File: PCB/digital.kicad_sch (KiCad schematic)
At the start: 34 parts, among them J13 JTAG, J14 FINAL_CARRERA_UP, J15 FINAL_CARRERA_DOWN, J3 ICSP, J4 CAN, J6 USART, J7 SPI, J8 RFID_COAX, U2 PIC32MK0256MCJ048-I/Y8X, U3 TCAN334D, Y1 ECS-3225SMV-080-GP-TR, Y2 ECS-3225SMV-080-GP-TR

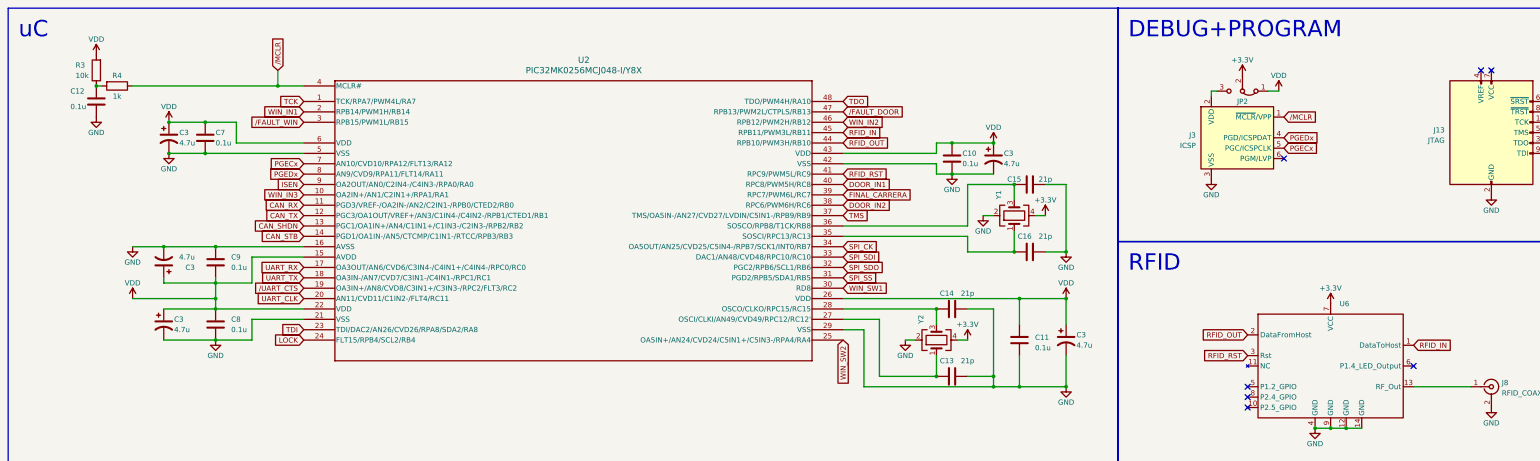
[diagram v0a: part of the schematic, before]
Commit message: power plane done
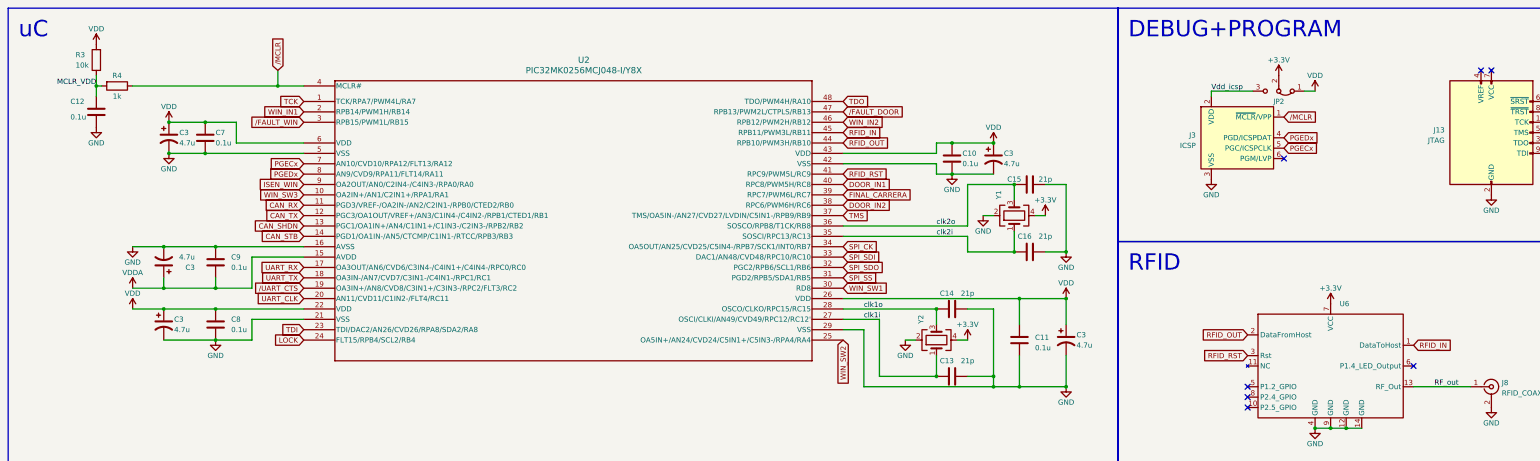
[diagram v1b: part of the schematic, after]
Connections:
- net VDD: no longer C3.1, C9.2, U2.15 (AVDD)
- net MCLR_VDD: now reaches C12.1, R3.1, R4.2
- net RF_out: now reaches J8.1 (In), U6.13 (RF_Out)
- net clk2i: now reaches C16.1, U2.35 (SOSCI/RPC13/RC13), Y1.1
- net clk2o: now reaches C15.1, U2.36 (SOSCO/RPB8/T1CK/RB8), Y1.3
- net clk1i: now reaches C13.1, U2.27 (OSCI/CLKI/AN49/CVD49/RPC12/RC12'), Y2.1
- net clk1o: now reaches C14.1, U2.28 (OSCO/CLKO/RPC15/RC15), Y2.3
- net Vdd_icsp: now reaches J3.2 (VDD), JP2.3 (B)
- net ISEN renamed ISEN_WIN
- net WIN_IN3 renamed WIN_SW3
- new net VDDA: C3.1, C9.2, U2.15 (AVDD)
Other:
- moved on the sheet: C12, JP2, R3

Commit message: start digital
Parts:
- added R1 (x2): 0, symbol Device:R
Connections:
- net GND: now also R1.2; no longer C3.2, C9.1, U2.16 (AVSS)
- net VDD: now also R1.2
- net VDDA: now also R1.1
- new net GNDA: C3.2, C9.1, R1.1, U2.16 (AVSS)
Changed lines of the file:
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@@
+    (fill (type none))
+  )
+  (rectangle (start 12.7 104.14) (end 34.29 129.54)
+    (stroke (width 0) (type default))
     (fill (type none))
   )
@@
     )
   )
+  (symbol (lib_id "Device:R") (at 22.86 113.03 90) (unit 1)
+    (in_bom yes) (on_board yes) (dnp no)
+    (property "Reference" "R1" (at 22.86 110.49 90)
+      (effects (font (size 1.27 1.27)))
+    )
+    (property "Value" "0" (at 22.86 115.57 90)
+      (effects (font (size 1.27 1.27)))
+    )
+    (property "Footprint" "" (at 22.86 114.808 90)
+      (effects (font (size 1.27 1.27)) hide)
+    )
+    (property "Datasheet" "~" (at 22.86 113.03 0)
+      (effects (font (size 1.27 1.27)) hide)
+    )
+    (pin "1")
+    (pin "2")
+    (instances
+      (project "DIJOUS_4_PORTES"
+        (path "/69b34976-047e-478e-bd76-9b6ef0dba356/0e58b9bb-7a32-4563-ae50-f5e325ba8348"
+          (reference "R1") (unit 1)
+        )
+        (path "/69b34976-047e-478e-bd76-9b6ef0dba356/6b83d062-cc2b-4223-9dc9-bddc64623104"
+          (reference "R2") (unit 1)
+        )
+      )
+    )
+  )
+  (symbol (lib_id "power:VDDA") (at 19.05 113.03 0) (unit 1)
+    (in_bom yes) (on_board yes) (dnp no) (fields_autoplaced)
+    (property "Reference" "#PWR08" (at 19.05 116.84 0)
+      (effects (font (size 1.27 1.27)) hide)
+    )
+    (property "Value" "VDDA" (at 19.05 109.22 0)
+      (effects (font (size 1.27 1.27)))
+    )
+    (property "Footprint" "" (at 19.05 113.03 0)
+      (effects (font (size 1.27 1.27)) hide)
+    )
+    (property "Datasheet" "" (at 19.05 113.03 0)
+      (effects (font (size 1.27 1.27)) hide)
+    )
+    (pin "1")
+    (instances
+      (project "DIJOUS_4_PORTES"
+        (path "/69b34976-047e-478e-bd76-9b6ef0dba356/6b83d062-cc2b-4223-9dc9-bddc64623104"
+          (reference "#PWR08") (unit 1)
+        )
+      )
+    )
+  )
   (symbol (lib_id "Device:R") (at 39.37 31.75 270) (unit 1)
     (in_bom yes) (on_board yes) (dnp no)
@@
         (path "/69b34976-047e-478e-bd76-9b6ef0dba356/6b83d062-cc2b-4223-9dc9-bddc64623104"
           (reference "R4") (unit 1)
-        )
-      )
-    )
-  )
-  (symbol (lib_id "power:GND") (at 43.18 71.12 0) (unit 1)
-    (in_bom yes) (on_board yes) (dnp no)
-    (property "Reference" "#PWR015" (at 43.18 77.47 0)
-      (effects (font (size 1.27 1.27)) hide)
-    )
-    (property "Value" "GND" (at 43.18 74.93 0)
-      (effects (font (size 1.27 1.27)))
-    )
-    (property "Footprint" "" (at 43.18 71.12 0)
-      (effects (font (size 1.27 1.27)) hide)
-    )
-    (property "Datasheet" "" (at 43.18 71.12 0)
-      (effects (font (size 1.27 1.27)) hide)
-    )
-    (pin "1")
-    (instances
-      (project "DIJOUS_4_PORTES"
-        (path "/69b34976-047e-478e-bd76-9b6ef0dba356/6b83d062-cc2b-4223-9dc9-bddc64623104"
-          (reference "#PWR015") (unit 1)
         )
       )
@@
     )
   )
+  (symbol (lib_id "power:GNDA") (at 19.05 120.65 0) (unit 1)
+    (in_bom yes) (on_board yes) (dnp no)
+    (property "Reference" "#PWR07" (at 19.05 127 0)
+      (effects (font (size 1.27 1.27)) hide)
+    )
+    (property "Value" "GNDA" (at 19.05 124.46 0)
+      (effects (font (size 1.27 1.27)))
+    )
+    (property "Footprint" "" (at 19.05 120.65 0)
+      (effects (font (size 1.27 1.27)) hide)
+    )
+    (property "Datasheet" "" (at 19.05 120.65 0)
+      (effects (font (size 1.27 1.27)) hide)
+    )
+    (pin "1")
+    (instances
+      (project "DIJOUS_4_PORTES"
+        (path "/69b34976-047e-478e-bd76-9b6ef0dba356/6b83d062-cc2b-4223-9dc9-bddc64623104"
+          (reference "#PWR07") (unit 1)
+        )
+      )
+    )
+  )
   (symbol (lib_id "power:GND") (at 271.78 105.41 0) (unit 1)
     (in_bom yes) (on_board yes) (dnp no)
@@
         (path "/69b34976-047e-478e-bd76-9b6ef0dba356/6b83d062-cc2b-4223-9dc9-bddc64623104"
           (reference "C29") (unit 1)
+        )
+      )
+    )
+  )
+  (symbol (lib_id "power:GND") (at 26.67 120.65 0) (unit 1)
+    (in_bom yes) (on_board yes) (dnp no)
+    (property "Reference" "#PWR09" (at 26.67 127 0)
+      (effects (font (size 1.27 1.27)) hide)
+    )
+    (property "Value" "GND" (at 26.67 124.46 0)
+      (effects (font (size 1.27 1.27)))
+    )
+    (property "Footprint" "" (at 26.67 120.65 0)
+      (effects (font (size 1.27 1.27)) hide)
+    )
+    (property "Datasheet" "" (at 26.67 120.65 0)
+      (effects (font (size 1.27 1.27)) hide)
+    )
+    (pin "1")
+    (instances
+      (project "DIJOUS_4_PORTES"
+        (path "/69b34976-047e-478e-bd76-9b6ef0dba356/6b83d062-cc2b-4223-9dc9-bddc64623104"
+          (reference "#PWR09") (unit 1)
         )
       )
@@
         (path "/69b34976-047e-478e-bd76-9b6ef0dba356/6b83d062-cc2b-4223-9dc9-bddc64623104"
           (reference "J3") (unit 1)
+        )
+      )
+    )
+  )
+  (symbol (lib_id "power:VDD") (at 26.67 113.03 0) (unit 1)
+    (in_bom yes) (on_board yes) (dnp no)
+    (property "Reference" "#PWR015" (at 26.67 116.84 0)
+      (effects (font (size 1.27 1.27)) hide)
+    )
+    (property "Value" "VDD" (at 26.67 109.22 0)
+      (effects (font (size 1.27 1.27)))
+    )
+    (property "Footprint" "" (at 26.67 113.03 0)
+      (effects (font (size 1.27 1.27)) hide)
+    )
+    (property "Datasheet" "" (at 26.67 113.03 0)
+      (effects (font (size 1.27 1.27)) hide)
+    )
+    (pin "1")
+    (instances
+      (project "DIJOUS_4_PORTES"
+        (path "/69b34976-047e-478e-bd76-9b6ef0dba356/6b83d062-cc2b-4223-9dc9-bddc64623104"
+          (reference "#PWR015") (unit 1)
         )
       )
@@
         )
       )
+    )
+  )
+  (symbol (lib_id "power:GNDA") (at 43.18 71.12 0) (unit 1)
+    (in_bom yes) (on_board yes) (dnp no)
+    (property "Reference" "#PWR04" (at 43.18 77.47 0)
+      (effects (font (size 1.27 1.27)) hide)
+    )
+    (property "Value" "GNDA" (at 43.18 74.93 0)
+      (effects (font (size 1.27 1.27)))
+    )
+    (property "Footprint" "" (at 43.18 71.12 0)
+      (effects (font (size 1.27 1.27)) hide)
+    )
+    (property "Datasheet" "" (at 43.18 71.12 0)
+      (effects (font (size 1.27 1.27)) hide)
+    )
+    (pin "1")
+    (instances
+      (project "DIJOUS_4_PORTES"
+        (path "/69b34976-047e-478e-bd76-9b6ef0dba356/6b83d062-cc2b-4223-9dc9-bddc64623104"
+          (reference "#PWR04") (unit 1)
+        )
+      )
+    )
+  )
+  (symbol (lib_id "Device:R") (at 22.86 120.65 90) (unit 1)
+    (in_bom yes) (on_board yes) (dnp no)
+    (property "Reference" "R1" (at 22.86 118.11 90)
+      (effects (font (size 1.27 1.27)))
+    )
+    (property "Value" "0" (at 22.86 123.19 90)
+      (effects (font (size 1.27 1.27)))
+    )
+    (property "Footprint" "" (at 22.86 122.428 90)
+      (effects (font (size 1.27 1.27)) hide)
+    )
+    (property "Datasheet" "~" (at 22.86 120.65 0)
+      (effects (font (size 1.27 1.27)) hide)
+    )
+    (pin "1")
+    (pin "2")
+    (instances
+      (project "DIJOUS_4_PORTES"
+        (path "/69b34976-047e-478e-bd76-9b6ef0dba356/0e58b9bb-7a32-4563-ae50-f5e325ba8348"
+          (reference "R1") (unit 1)
+        )
+        (path "/69b34976-047e-478e-bd76-9b6ef0dba356/6b83d062-cc2b-4223-9dc9-bddc64623104"
+          (reference "R9") (unit 1)
+        )
+      )

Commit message: changed clks, pwr
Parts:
- removed C13, C14, C15, C16: 21p, Capacitor_SMD:C_01005_0402Metric, symbol Device:C
- removed J13: JTAG, Connector_IDC:IDC-Header_2x05_P2.54mm_Vertical, symbol Connector:AVR-JTAG-10
- removed JP2: Jumper_3_Bridged12, Connector_PinHeader_1.00mm:PinHeader_1x03_P1.00mm_Vertical, symbol Jumper:Jumper_3_Bridged12
- removed R1 (x2): 0, symbol Device:R
- removed Y1, Y2: ECS-3225SMV-080-GP-TR, kicad_models:OSC_ECS-3225SMV-080-GP-TR, symbol Device:Crystal_GND24
- added Y1: ASZKDV-32.768KHZ-L-T3, kicad_models:ASZKDV_ABR, symbol ASZKDV_ABR:ASZKDV-32.768KHZ-L-T3
- added Y2: ECS-3225SMV-080-GP-TR, kicad_models:OSC_ECS-3225SMV-080-GP-TR, symbol ECS-3225SMV-080-GP-TR:ECS-3225SMV-080-GP-TR
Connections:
- net FINAL_CARRERA is gone; now on net FINAL_CARRERA_UP: U2.39 (RPC7/PWM6L/RC7)
- net GNDA is gone; now on net GND: C3.2, C9.1, U2.16 (AVSS)
- net VDD is gone; now on net +3.3V: C10.1, C11.1, C3.1, C3.1, C3.1, C3.1, C7.1, C8.1, R3.2, U2.22 (VDD), U2.26 (VDD), U2.43 (VDD), U2.6 (VDD)
- net VDDA is gone; now on net +3.3V: C3.1, C9.2, U2.15 (AVDD)
- net Vdd_icsp is gone; now on net +3.3V: J3.2 (VDD)
- net clk2o is gone; now on net FINAL_CARRERA_DOWN: U2.36 (SOSCO/RPB8/T1CK/RB8)
- net +3.3V: now also Y1.3 (OE), Y1.4 (VDD), Y2.4 (VDD)
- net GND: now also Y1.2 (GND), Y2.2 (GND)
- net clk1i: now also Y2.3 (OUTPUT)
- net clk2i: now also Y1.1 (OUTPUT)
- net clk1o: no longer names the net of U2.28 (OSCO/CLKO/RPC15/RC15)
- no-connect marks 16 -> 15
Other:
- moved on the sheet: C11, C3

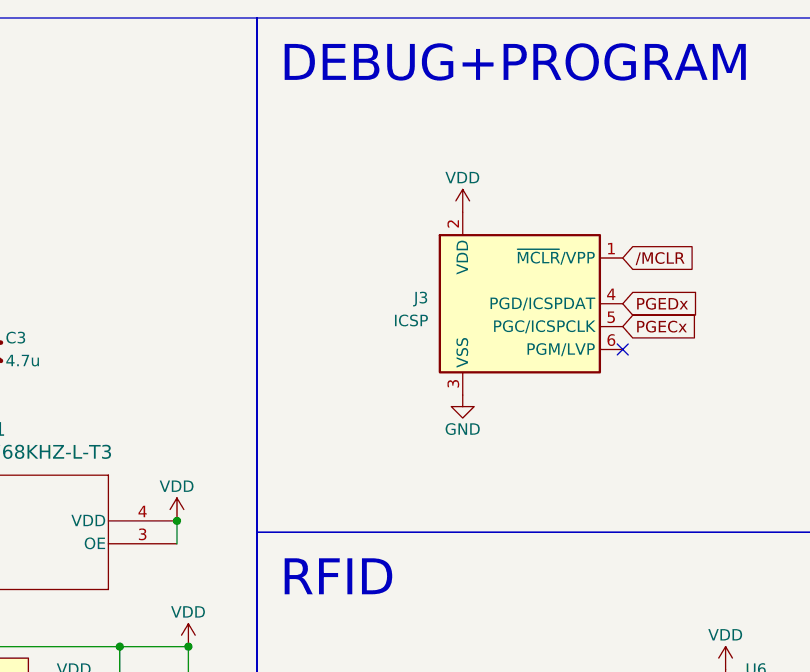
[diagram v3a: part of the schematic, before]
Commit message: canvis a sortides de potencia
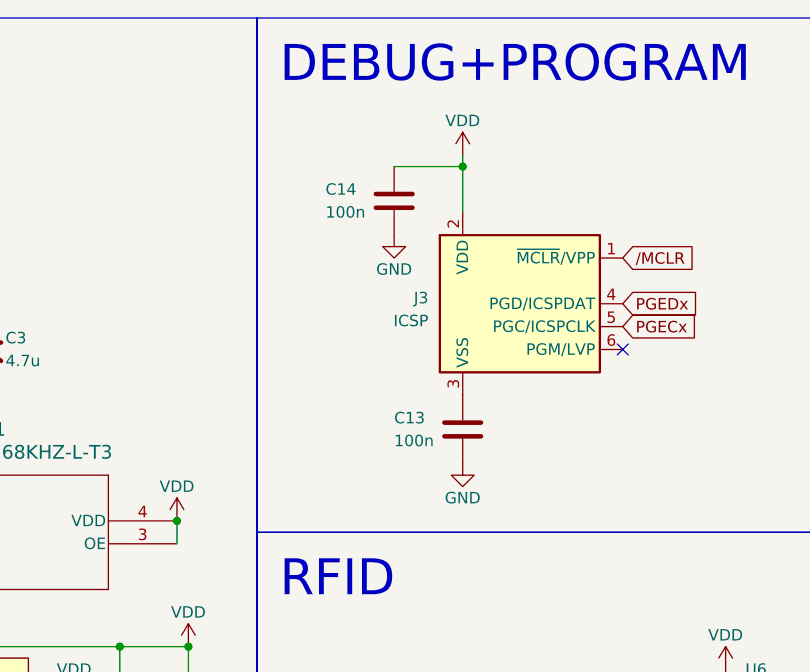
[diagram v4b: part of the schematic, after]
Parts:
- added C13, C14: 100n, Capacitor_SMD:C_0805_2012Metric, symbol Device:C
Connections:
- net +3.3V: now also C14.2
- net GND: now also C13.1, C14.1; no longer J3.3 (VSS)
- new net: C13.2, J3.3 (VSS)
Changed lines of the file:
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@@
   (junction (at 254 45.72) (diameter 0) (color 0 0 0 0)
+  )
+  (junction (at 307.34 29.21) (diameter 0) (color 0 0 0 0)
   )
   (junction (at 336.55 115.57) (diameter 0) (color 0 0 0 0)
@@
     (stroke (width 0) (type default))
   )
+  (wire (pts (xy 307.34 29.21) (xy 307.34 34.29))
+    (stroke (width 0) (type default))
+  )
   (wire (pts (xy 19.05 120.65) (xy 26.67 120.65))
     (stroke (width 0) (type default))
@@
     (stroke (width 0) (type default))
   )
+  (wire (pts (xy 299.72 29.21) (xy 307.34 29.21))
+    (stroke (width 0) (type default))
+  )
   (wire (pts (xy 34.29 29.21) (xy 34.29 31.75))
     (stroke (width 0) (type default))
@@
   )
   (wire (pts (xy 68.58 40.64) (xy 68.58 45.72))
+    (stroke (width 0) (type default))
+  )
+  (wire (pts (xy 307.34 27.94) (xy 307.34 29.21))
     (stroke (width 0) (type default))
   )
@@
     )
   )
+  (symbol (lib_id "power:GND") (at 299.72 36.83 0) (unit 1)
+    (in_bom yes) (on_board yes) (dnp no)
+    (property "Reference" "#PWR029" (at 299.72 43.18 0)
+      (effects (font (size 1.27 1.27)) hide)
+    )
+    (property "Value" "GND" (at 299.72 40.64 0)
+      (effects (font (size 1.27 1.27)))
+    )
+    (property "Footprint" "" (at 299.72 36.83 0)
+      (effects (font (size 1.27 1.27)) hide)
+    )
+    (property "Datasheet" "" (at 299.72 36.83 0)
+      (effects (font (size 1.27 1.27)) hide)
+    )
+    (pin "1")
+    (instances
+      (project "DIJOUS_4_PORTES"
+        (path "/69b34976-047e-478e-bd76-9b6ef0dba356/6b83d062-cc2b-4223-9dc9-bddc64623104"
+          (reference "#PWR029") (unit 1)
+        )
+      )
+    )
+  )
   (symbol (lib_id "Device:R") (at 39.37 31.75 270) (unit 1)
     (in_bom yes) (on_board yes) (dnp no)
@@
         (path "/69b34976-047e-478e-bd76-9b6ef0dba356/6b83d062-cc2b-4223-9dc9-bddc64623104"
           (reference "R3") (unit 1)
+        )
+      )
+    )
+  )
+  (symbol (lib_id "Device:C") (at 307.34 58.42 180) (unit 1)
+    (in_bom yes) (on_board yes) (dnp no)
+    (property "Reference" "C13" (at 299.72 57.15 0)
+      (effects (font (size 1.27 1.27)) (justify right))
+    )
+    (property "Value" "100n" (at 299.72 59.69 0)
+      (effects (font (size 1.27 1.27)) (justify right))
+    )
+    (property "Footprint" "Capacitor_SMD:C_0805_2012Metric" (at 306.3748 54.61 0)
+      (effects (font (size 1.27 1.27)) hide)
+    )
+    (property "Datasheet" "~" (at 307.34 58.42 0)
+      (effects (font (size 1.27 1.27)) hide)
+    )
+    (pin "1")
+    (pin "2")
+    (instances
+      (project "DIJOUS_4_PORTES"
+        (path "/69b34976-047e-478e-bd76-9b6ef0dba356/6b83d062-cc2b-4223-9dc9-bddc64623104"
+          (reference "C13") (unit 1)
         )
       )
@@
     )
   )
+  (symbol (lib_id "Device:C") (at 299.72 33.02 180) (unit 1)
+    (in_bom yes) (on_board yes) (dnp no)
+    (property "Reference" "C14" (at 292.1 31.75 0)
+      (effects (font (size 1.27 1.27)) (justify right))
+    )
+    (property "Value" "100n" (at 292.1 34.29 0)
+      (effects (font (size 1.27 1.27)) (justify right))
+    )
+    (property "Footprint" "Capacitor_SMD:C_0805_2012Metric" (at 298.7548 29.21 0)
+      (effects (font (size 1.27 1.27)) hide)
+    )
+    (property "Datasheet" "~" (at 299.72 33.02 0)
+      (effects (font (size 1.27 1.27)) hide)
+    )
+    (pin "1")
+    (pin "2")
+    (instances
+      (project "DIJOUS_4_PORTES"
+        (path "/69b34976-047e-478e-bd76-9b6ef0dba356/6b83d062-cc2b-4223-9dc9-bddc64623104"
+          (reference "C14") (unit 1)
+        )
+      )
+    )
+  )
   (symbol (lib_id "Device:C_Polarized_US") (at 50.8 90.17 0) (unit 1)
     (in_bom yes) (on_board yes) (dnp no)
@@
     )
   )
-  (symbol (lib_id "power:VDD") (at 307.34 34.29 0) (unit 1)
-    (in_bom yes) (on_board yes) (dnp no)
-    (property "Reference" "#PWR025" (at 307.34 38.1 0)
-      (effects (font (size 1.27 1.27)) hide)
-    )
-    (property "Value" "VDD" (at 307.34 30.48 0)
-      (effects (font (size 1.27 1.27)))
-    )
-    (property "Footprint" "" (at 307.34 34.29 0)
-      (effects (font (size 1.27 1.27)) hide)
-    )
-    (property "Datasheet" "" (at 307.34 34.29 0)
+  (symbol (lib_id "power:VDD") (at 307.34 27.94 0) (unit 1)
+    (in_bom yes) (on_board yes) (dnp no)
+    (property "Reference" "#PWR025" (at 307.34 31.75 0)
+      (effects (font (size 1.27 1.27)) hide)
+    )
+    (property "Value" "VDD" (at 307.34 24.13 0)
+      (effects (font (size 1.27 1.27)))
+    )
+    (property "Footprint" "" (at 307.34 27.94 0)
+      (effects (font (size 1.27 1.27)) hide)
+    )
+    (property "Datasheet" "" (at 307.34 27.94 0)
       (effects (font (size 1.27 1.27)) hide)
     )
@@
     )
   )
-  (symbol (lib_id "power:GND") (at 307.34 54.61 0) (unit 1)
-    (in_bom yes) (on_board yes) (dnp no)
-    (property "Reference" "#PWR026" (at 307.34 60.96 0)
-      (effects (font (size 1.27 1.27)) hide)
-    )
-    (property "Value" "GND" (at 307.34 58.42 0)
-      (effects (font (size 1.27 1.27)))
-    )
-    (property "Footprint" "" (at 307.34 54.61 0)
-      (effects (font (size 1.27 1.27)) hide)
-    )
-    (property "Datasheet" "" (at 307.34 54.61 0)
-      (effects (font (size 1.27 1.27)) hide)
-    )
+  (symbol (lib_id "power:GND") (at 307.34 62.23 0) (unit 1)
+    (in_bom yes) (on_board yes) (dnp no)
+    (property "Reference" "#PWR026" (at 307.34 68.58 0)
+      (effects (font (size 1.27 1.27)) hide)
+    )
+    (property "Value" "GND" (at 307.34 66.04 0)
+      (effects (font (size 1.27 1.27)))
+    )
+    (property "Footprint" "" (at 307.34 62.23 0)
+      (effects (font (size 1.27 1.27)) hide)
+    )
+    (property "Datasheet" "" (at 307.34 62.23 0)
+      (effects (font (size 1.27 1.27)) hide)
+    )
